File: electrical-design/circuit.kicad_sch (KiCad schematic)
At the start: 33 parts

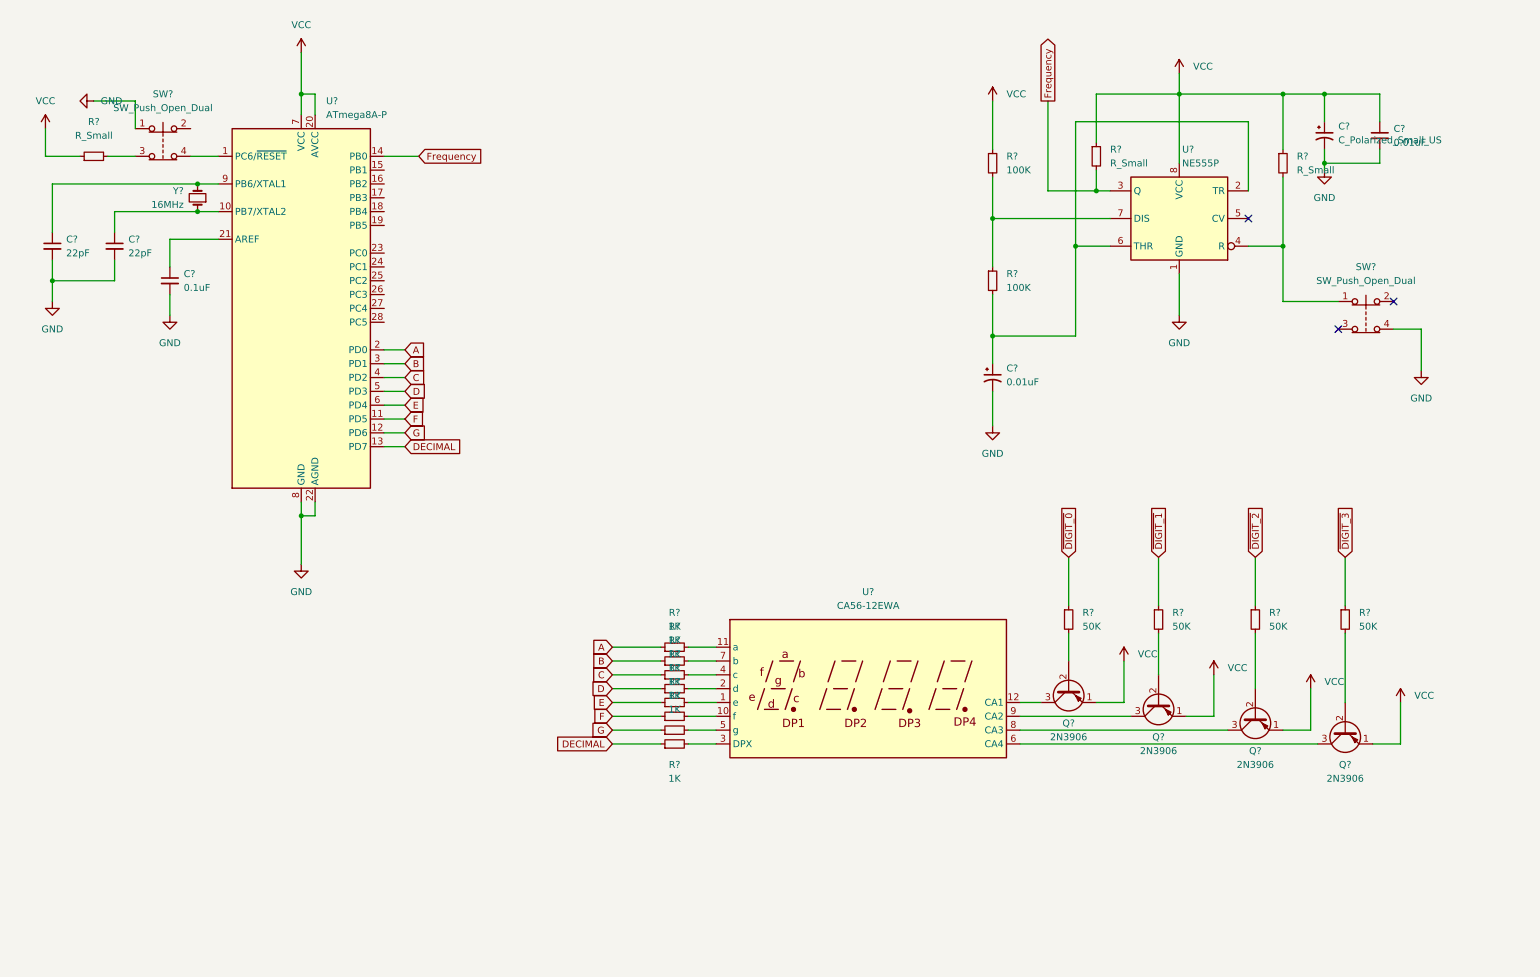
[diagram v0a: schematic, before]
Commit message: Moving Away From Protoboard to Actual PCB Due to Production Complications
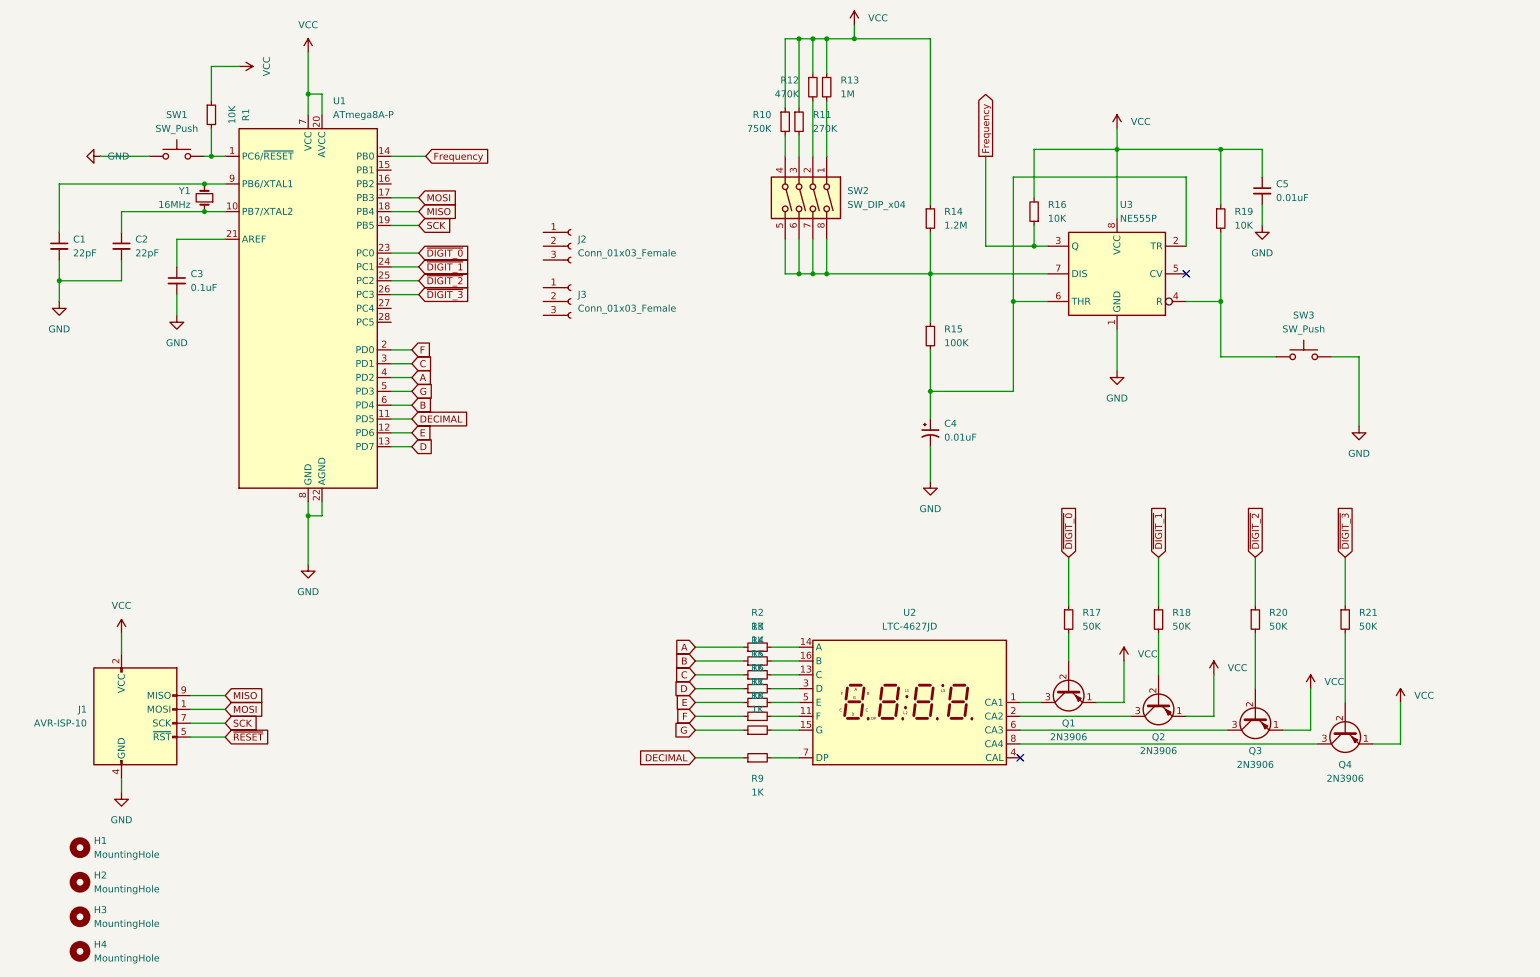
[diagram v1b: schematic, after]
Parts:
- removed C?: C_Polarized_Small_US, symbol Device:C_Polarized_Small_US
- removed C?: 0.01uF, symbol Device:C_Small
- removed R?: R_Small, symbol Device:R_Small
- removed SW? (x2): SW_Push_Open_Dual, symbol Switch:SW_Push_Open_Dual
- removed U?: CA56-12EWA, Display_7Segment:CA56-12EWA, symbol Display_Character:CA56-12EWA
- added C5: 0.01uF, Capacitor_THT:C_Disc_D3.0mm_W2.0mm_P2.50mm, symbol Device:C_Small
- added H1, H2, H3, H4: MountingHole, MountingHole:MountingHole_2.2mm_M2_DIN965_Pad_TopBottom, symbol Mechanical:MountingHole
- added J1: AVR-ISP-10, Connector_IDC:IDC-Header_2x05_P2.54mm_Vertical, symbol Connector:AVR-ISP-10
- added J2, J3: Conn_01x03_Female, Connector_JST:JST_XH_B3B-XH-A_1x03_P2.50mm_Vertical, symbol Connector:Conn_01x03_Female
- added R1: 10K, Resistor_THT:R_Axial_DIN0204_L3.6mm_D1.6mm_P5.08mm_Horizontal, symbol Device:R_Small
- added R10: 750K, Resistor_THT:R_Axial_DIN0204_L3.6mm_D1.6mm_P5.08mm_Horizontal, symbol Device:R_Small
- added R11: 270K, Resistor_THT:R_Axial_DIN0204_L3.6mm_D1.6mm_P5.08mm_Horizontal, symbol Device:R_Small
- added R12: 470K, Resistor_THT:R_Axial_DIN0204_L3.6mm_D1.6mm_P5.08mm_Horizontal, symbol Device:R_Small
- added R13: 1M, Resistor_THT:R_Axial_DIN0204_L3.6mm_D1.6mm_P5.08mm_Horizontal, symbol Device:R_Small
- added SW1, SW3: SW_Push, Button_Switch_THT:SW_PUSH_6mm_H5mm, symbol Switch:SW_Push
- added SW2: SW_DIP_x04, Button_Switch_THT:SW_DIP_SPSTx04_Slide_9.78x12.34mm_W7.62mm_P2.54mm, symbol Switch:SW_DIP_x04
- added U2: LTC-4627JD, Display_7Segment:LTC-4627Jx, symbol Display_Character:LTC-4627JD
- C4: renamed from C?; footprint (none) -> Capacitor_THT:C_Disc_D3.0mm_W2.0mm_P2.50mm
- R14: renamed from R?; value 100K -> 1.2M; footprint (none) -> Resistor_THT:R_Axial_DIN0204_L3.6mm_D1.6mm_P5.08mm_Horizontal
- R15, R17, R18, R2, R20, R21, R3, R4, R5, R6, R7, R8, R9: renamed from R?; footprint (none) -> Resistor_THT:R_Axial_DIN0204_L3.6mm_D1.6mm_P5.08mm_Horizontal
- R16, R19: renamed from R?; value R_Small -> 10K; footprint (none) -> Resistor_THT:R_Axial_DIN0204_L3.6mm_D1.6mm_P5.08mm_Horizontal
- Y1: renamed from Y?; footprint (none) -> Crystal:Crystal_HC49-4H_Vertical
- gave numbers to parts that had none: 9
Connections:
- net A: now also U1.4 (PD2); no longer U1.2 (PD0)
- net B: now also U1.6 (PD4); no longer U1.3 (PD1)
- net C: now also U1.3 (PD1); no longer U1.4 (PD2)
- net D: now also U1.13 (PD7); no longer U1.5 (PD3)
- net DECIMAL: now also U1.11 (PD5); no longer U1.13 (PD7)
- net E: now also U1.12 (PD6); no longer U1.6 (PD4)
- net F: now also U1.2 (PD0); no longer U1.11 (PD5)
- net Frequency: now also R16.1; no longer R16.2
- net G: now also U1.5 (PD3); no longer U1.12 (PD6)
- net GND: now also C5.2, J1.10 (GND), J1.4 (GND), J1.6 (GND), J1.8 (GND), SW1.1, SW3.2
- net VCC: now also R16.2, C5.1, J1.2 (VCC), R1.1, R10.1, R11.1, R12.1, R13.1; no longer R16.1
- net ~{DIGIT_0}: now also U1.23 (PC0)
- net ~{DIGIT_1}: now also U1.24 (PC1)
- net ~{DIGIT_2}: now also U1.25 (PC2)
- net ~{DIGIT_3}: now also U1.26 (PC3)
- net at R7.2: now also U2.11 (F)
- net at U1.1 (PC6/~{RESET}): now also R1.2, SW1.2
- net MOSI: now reaches U1.17 (PB3)
- net MOSI: now also J1.1 (MOSI)
- net MISO: now reaches U1.18 (PB4)
- net MISO: now also J1.9 (MISO)
- net SCK: now reaches U1.19 (PB5)
- net SCK: now also J1.7 (SCK)
- net at R2.2: now also U2.14 (A)
- net at R4.2: now also U2.13 (C)
- net at Q2.3 (C): now also U2.2 (CA2)
- net at R19.2, U3.4 (R): now also SW3.1
- net at R3.2: now also U2.16 (B)
- net at R14.2, R15.1, U3.7 (DIS): now also SW2.5, SW2.6, SW2.7, SW2.8
- net at Q4.3 (C): now also U2.8 (CA4)
- net at R5.2: now also U2.3 (D)
- net at R6.2: now also U2.5 (E)
- net at R8.2: now also U2.15 (G)
- net at Q1.3 (C): now also U2.1 (CA1)
- net at R9.2: now also U2.7 (DP)
- net at Q3.3 (C): now also U2.6 (CA3)
- new net: R13.2, SW2.1
- new net: R12.2, SW2.2
- new net: R11.2, SW2.3
- new net: R10.2, SW2.4
- new net ~{RESET}: J1.5 (~{RST})
- no-connect marks 3 -> 2
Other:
- moved on the sheet: C1, C2, C3, C4, R14, R15, R16, R19, R2, R3, R4, R5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

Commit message: Added LED's to Board
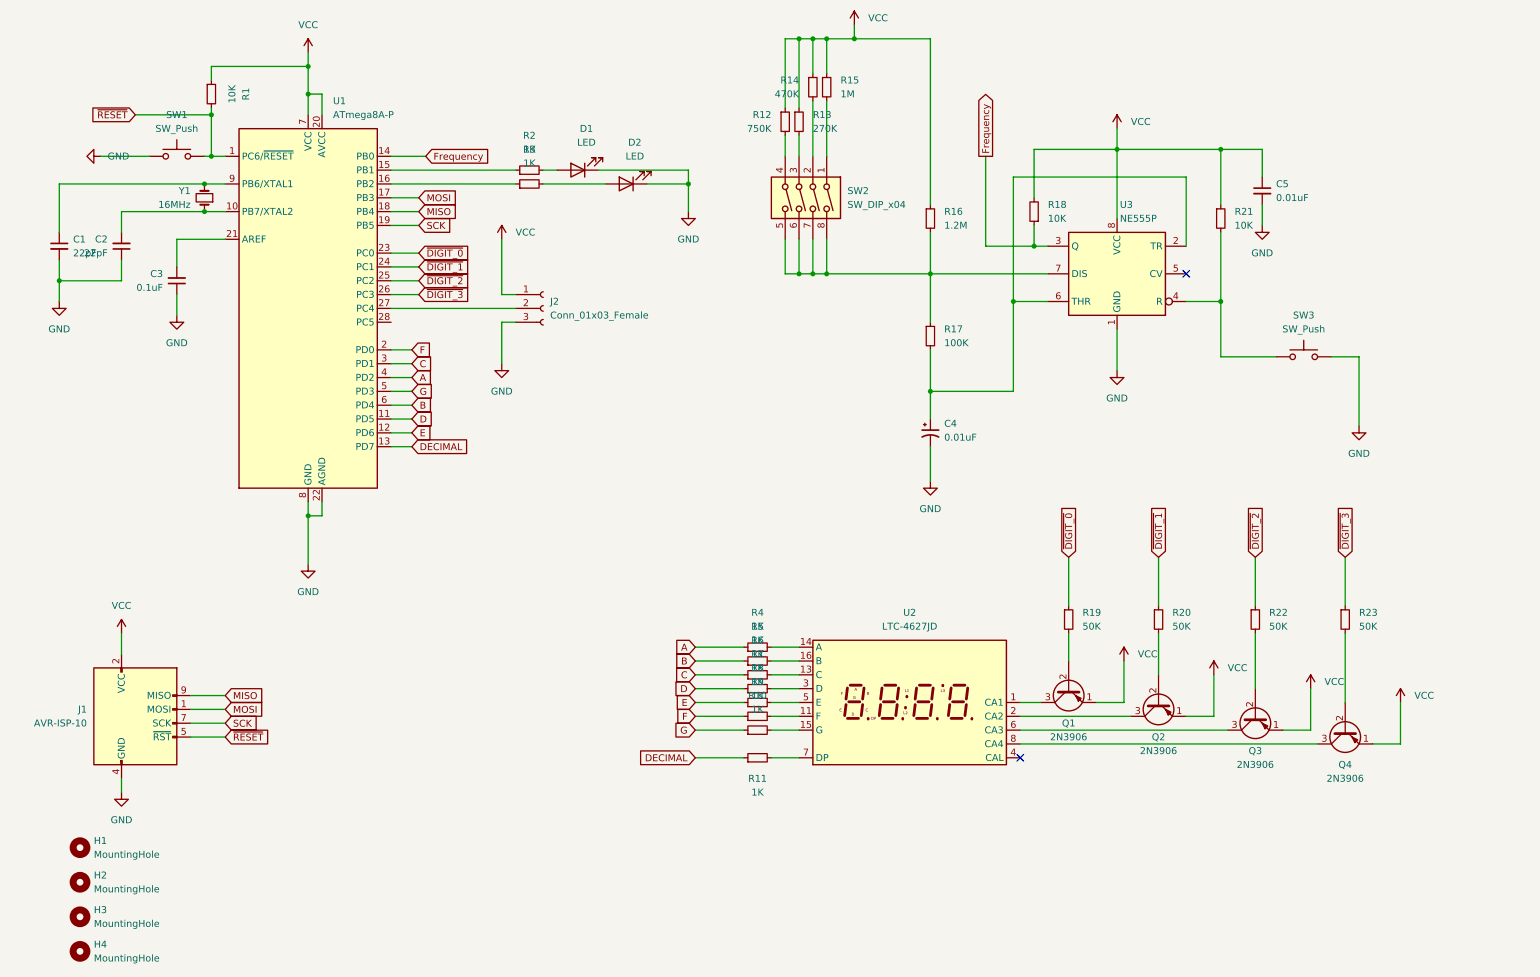
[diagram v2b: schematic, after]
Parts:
- removed J3: Conn_01x03_Female, Connector_JST:JST_XH_B3B-XH-A_1x03_P2.50mm_Vertical, symbol Connector:Conn_01x03_Female
- added D1, D2: LED, LED_THT:LED_D3.0mm, symbol Device:LED
- added R2, R3: 1K, Resistor_THT:R_Axial_DIN0204_L3.6mm_D1.6mm_P5.08mm_Horizontal, symbol Device:R_Small
- C1, C2, C3: footprint (none) -> Capacitor_THT:C_Disc_D3.0mm_W2.0mm_P2.50mm
- renumbered R8 to R10, R9 to R11, R10 to R12, R11 to R13, R12 to R14, R13 to R15, R14 to R16, R15 to R17, R16 to R18, R17 to R19, R18 to R20, R19 to R21, R20 to R22, R21 to R23, R2 to R4, R3 to R5, R4 to R6, R5 to R7, R6 to R8, R7 to R9
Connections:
- net D: now also U1.11 (PD5); no longer U1.13 (PD7)
- net DECIMAL: now also U1.13 (PD7); no longer U1.11 (PD5)
- net GND: now also C2.1, C3.1, J2.3 (Pin_3), D1.1 (K), D2.1 (K); no longer C2.2, C3.2
- net VCC: now also J2.1 (Pin_1)
- net ~{RESET}: now also R1.2, SW1.2, U1.1 (PC6/~{RESET})
- net at U1.10 (PB7/XTAL2), Y1.1: now also C2.2; no longer C2.1
- net at U1.15 (PB1): now also R2.1
- net at U1.16 (PB2): now also R3.1
- net at U1.21 (AREF): now also C3.2; no longer C3.1
- net at U1.27 (PC4): now also J2.2 (Pin_2)
- new net: D2.2 (A), R3.2
- new net: D1.2 (A), R2.2
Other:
- moved on the sheet: J2, R1

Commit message: Completed Initial Design of Circuit Board
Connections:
- net Frequency: now also R18.2; no longer R18.1
- net GND: now also C3.2, R2.2, R3.2; no longer C3.1, D1.1 (K), D2.1 (K)
- net VCC: now also R18.1; no longer R18.2
- net at U1.15 (PB1): now also D1.2 (A); no longer R2.1
- net at U1.16 (PB2): now also D2.2 (A); no longer R3.1
- net at U1.21 (AREF): now also C3.1; no longer C3.2
- net at SW2.1: now also R16.2, R17.1, SW2.2, SW2.3, SW2.4, U3.7 (DIS); no longer R15.2
- net at R14.2: now also SW2.6; no longer SW2.2
- net at R13.2: now also SW2.7; no longer SW2.3
- net at R12.2: now also SW2.8; no longer SW2.4
- net DECIMAL renamed DEC
- new net: R15.2, SW2.5
- new net: D2.1 (K), R3.1
- new net: D1.1 (K), R2.1
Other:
- moved on the sheet: D2, H1, H2, H3, H4, J1, Q1, Q2, Q3, Q4, R10, R11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

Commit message: Added Production Files
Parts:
- J2: value Conn_01x03_Female -> Analoge Header
- SW1, SW3: value SW_Push -> Reset Button

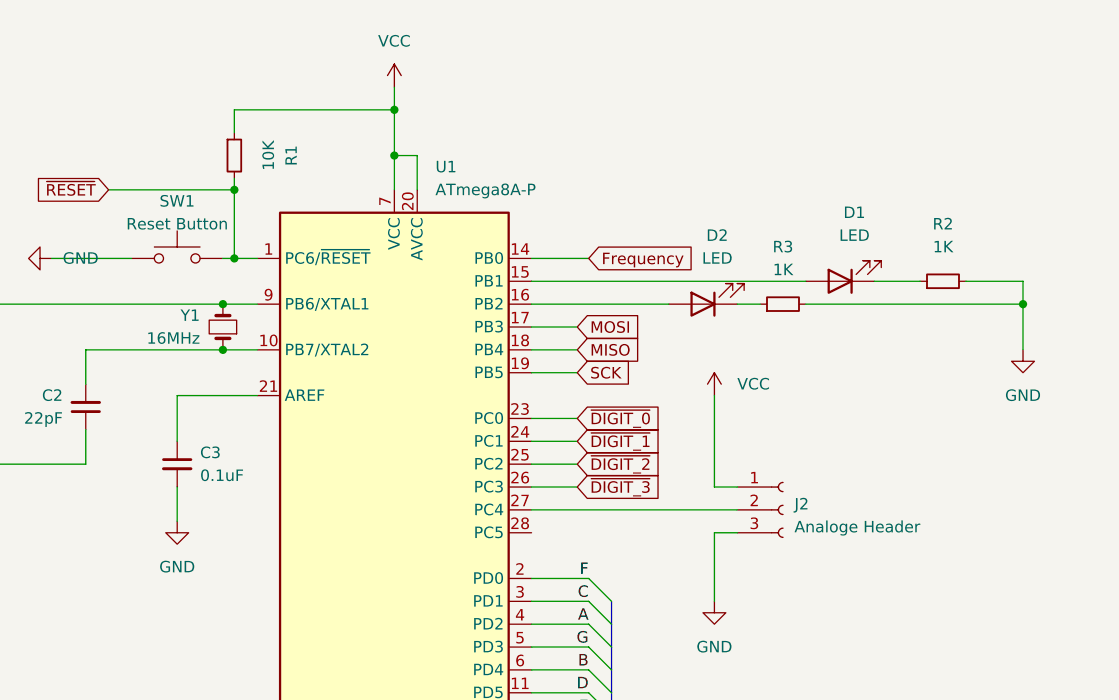
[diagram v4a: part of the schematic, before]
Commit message: Approved Evaluation Board For Production
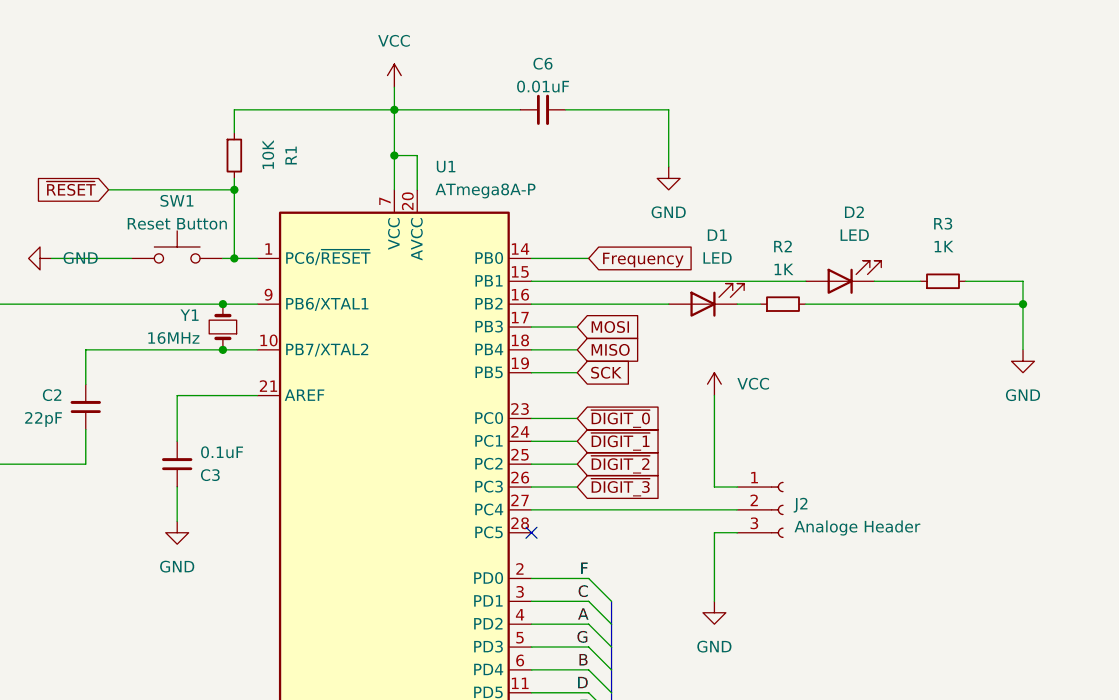
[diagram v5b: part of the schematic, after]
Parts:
- added C6: 0.01uF, Capacitor_THT:C_Disc_D3.0mm_W2.0mm_P2.50mm, symbol Device:C_Small
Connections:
- net GND: now also C3.1, C6.2; no longer C3.2
- net VCC: now also C6.1
- net at U1.15 (PB1): now also D2.2 (A); no longer D1.2 (A)
- net at U1.16 (PB2): now also D1.2 (A); no longer D2.2 (A)
- net at U1.21 (AREF): now also C3.2; no longer C3.1
- no-connect marks 2 -> 3
